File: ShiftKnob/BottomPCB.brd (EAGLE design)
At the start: 37.8 x 40.2 mm, 39 parts, among them IC2 UA78M05DCY, J1 AVR_SPI_PRG_6PTH, Q1 16MHz, Q2 MOSFET-NCHANNELSMD, Q3 MOSFET-PCHANNELSMD, Q4 MOSFET-NCHANNELSMD, Q5 MOSFET-NCHANNELSMD, Q6 MOSFET-NCHANNELSMD, U1 ATMEGA328, U3 FT232RL-BASICSSOP

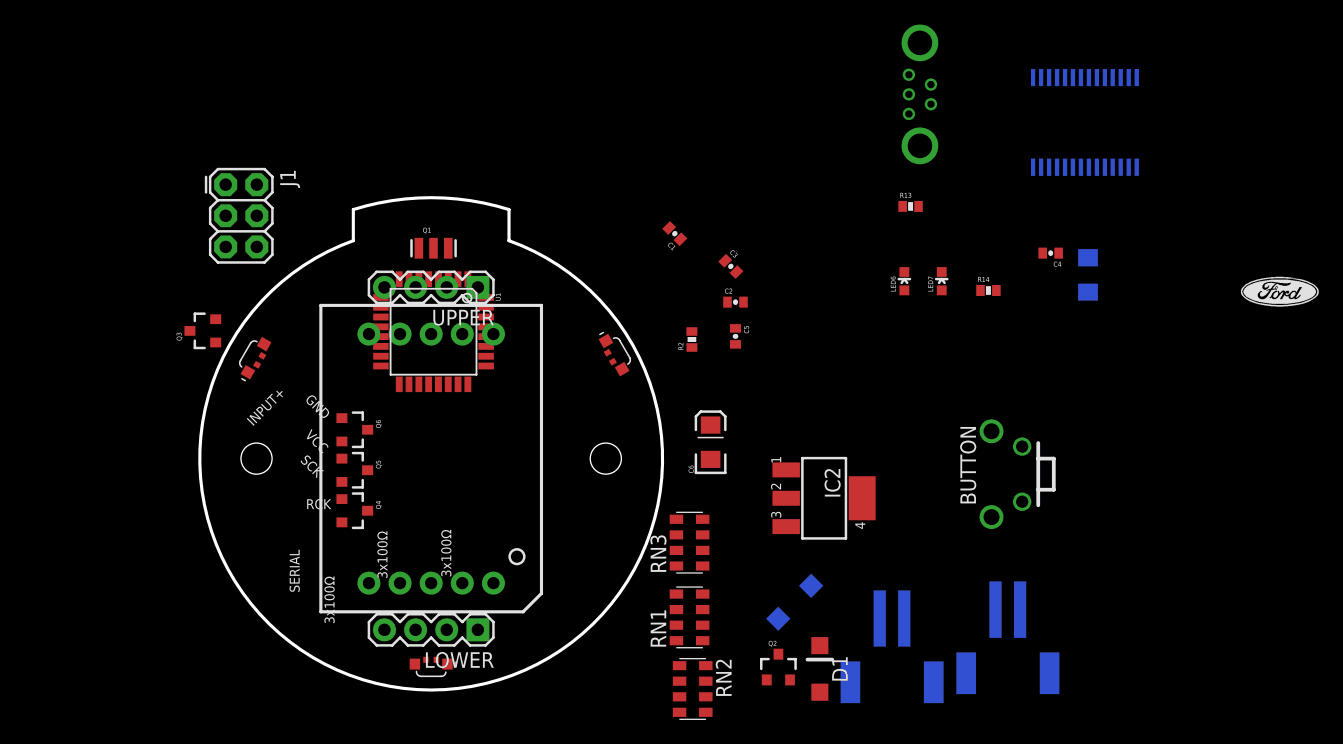
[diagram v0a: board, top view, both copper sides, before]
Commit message: swap out button for edge_mount button in Ford_frames library.
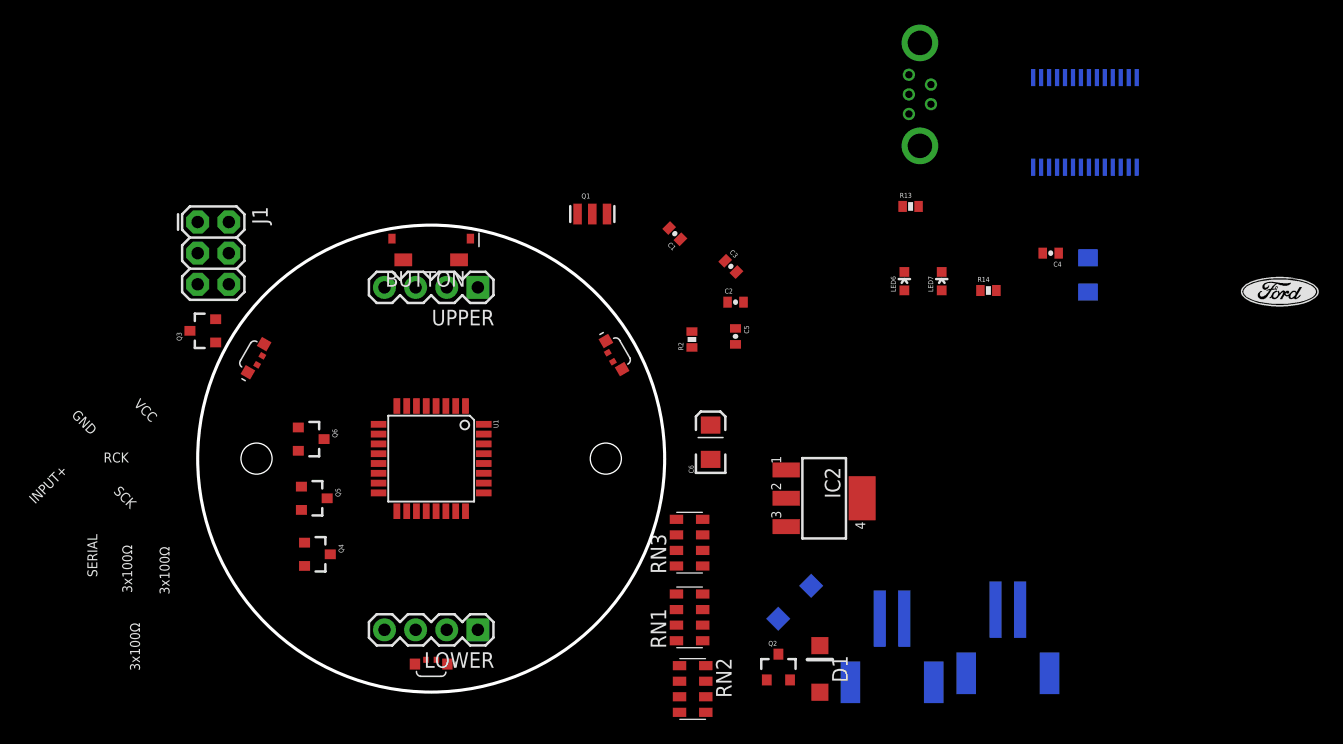
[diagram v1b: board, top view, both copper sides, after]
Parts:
- removed U$2: 7-SEGMENT-DISPLAY-1"-RED, SparkFun-Displays:7-SEGMENT-1"PTH
- BUTTON: value BUTTON_RIGHTANGLE_SMD -> BUTTON_EDGE; device FORD_frames:BUTTON_RIGHTANGLE -> FORD_frames:BUTTON_EDGE
- moved BUTTON 49.9 mm to (21.6, 40.4), turned to 180 degrees
- moved Q1 13.3 mm to (34.7, 41.5)
- moved U1 10.4 mm to (21.6, 21.6)
- moved Q4 4.68 mm to (12.3, 13.8)
- moved Q5 4.02 mm to (12.0, 18.4)
- moved J1 3.81 mm to (2.54, 40.9)
- moved Q6 3.64 mm to (11.8, 23.2)
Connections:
- net D2: now also BUTTON.P2; no longer BUTTON.PIN2
- net GND: now also BUTTON.P1; no longer BUTTON.PIN1
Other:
- board size 37.8 x 40.2 mm -> 38.1 x 38.1 mm

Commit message: everything on the board. need to route traces.
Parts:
- R13, R14: value 1K -> 10K
- moved U3 63.1 mm to (15.2, 28.7), flipped to the top, turned to 0 degrees
- moved C10 53.3 mm to (22.4, 29.2), flipped to the top, turned to 90 degrees
- moved R14 51.4 mm to (15.7, 37.8), turned to 180 degrees
- moved R13 49.0 mm to (12.2, 35.3), turned to 90 degrees
- moved C4 48.5 mm to (24.4, 30.0), turned to 90 degrees
- moved JP4 48.1 mm to (12.4, 16.0), turned to 0 degrees
- moved Q2 47.8 mm to (6.97, 25.4), turned to 180 degrees
- moved LED7 47.8 mm to (15.5, 35.3), turned to 180 degrees
- moved JP3 47.0 mm to (22.8, 15.8), turned to 0 degrees
- moved LED6 46.2 mm to (14.0, 35.3), turned to 180 degrees
- moved IC2 43.3 mm to (10.6, 13.7), turned to 90 degrees
- moved D1 40.7 mm to (12.8, 8.60), turned to 0 degrees
- moved D2 40.5 mm to (12.5, 21.7), flipped to the top, turned to 180 degrees
- moved J1 40.3 mm to (29.0, 10.4), turned to 0 degrees
- moved U$6 40.2 mm to (28.6, 28.1)
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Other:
- board text added: "02"
- board text removed: "01"

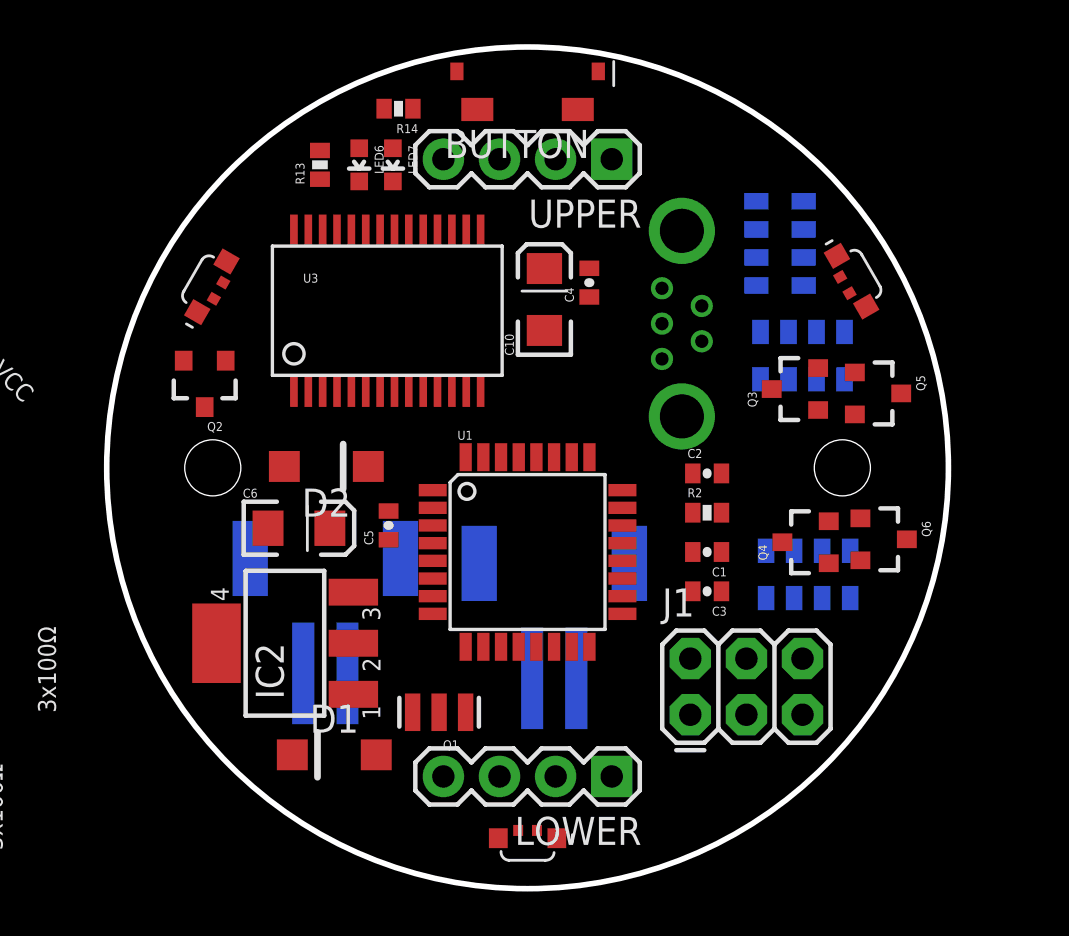
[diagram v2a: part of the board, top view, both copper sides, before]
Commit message: reworked the board layout. power traces complete.
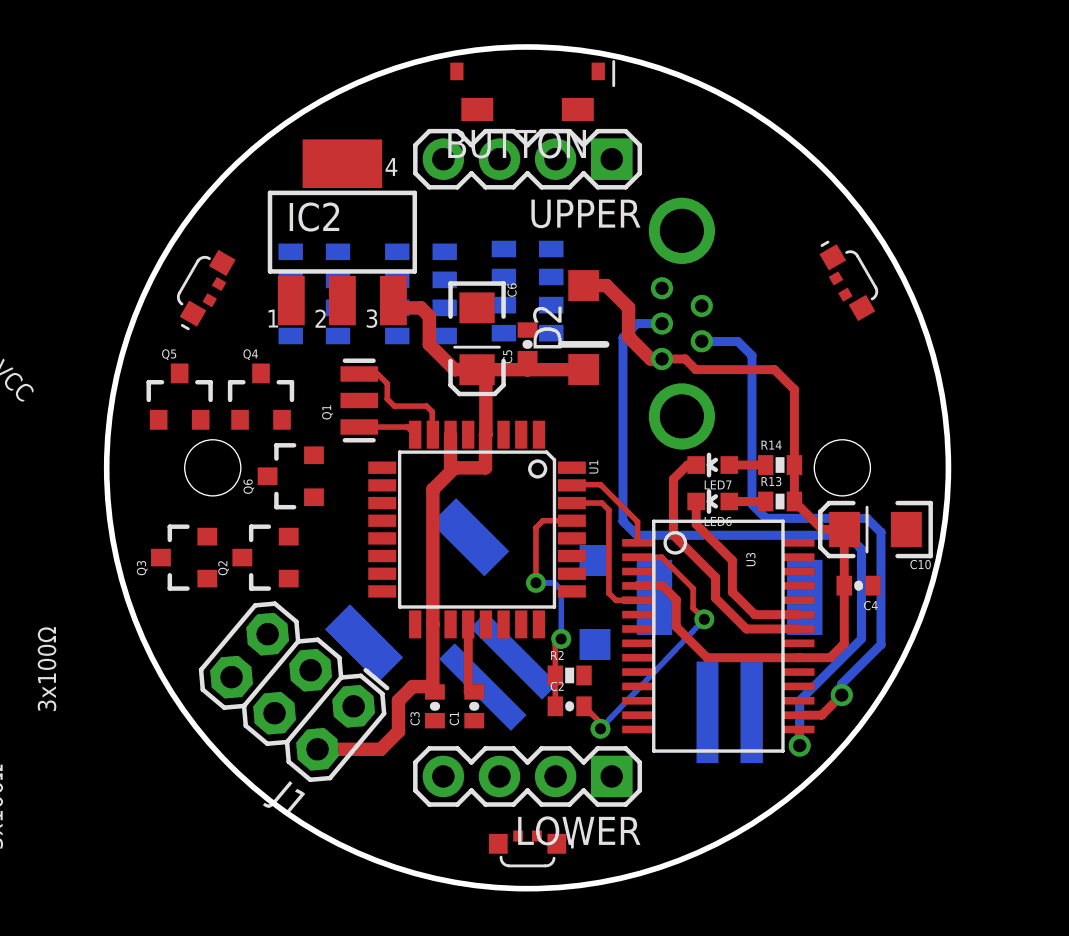
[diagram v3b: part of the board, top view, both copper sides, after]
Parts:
- moved Q5 31.6 mm to (5.84, 24.8), turned to 0 degrees
- moved Q3 28.7 mm to (6.10, 17.5)
- moved Q6 26.9 mm to (10.9, 21.2), turned to 90 degrees
- moved R13 25.8 mm to (33.0, 20.1), turned to 0 degrees
- moved Q4 25.6 mm to (9.53, 24.8), turned to 0 degrees
- moved R14 23.6 mm to (33.0, 21.7), turned to 0 degrees
- moved RN3 22.3 mm to (11.9, 29.5), turned to 90 degrees
- moved LED6 22.1 mm to (30.0, 20.1), turned to 90 degrees
- moved U3 21.0 mm to (30.2, 14.0), turned to 270 degrees
- moved LED7 19.9 mm to (30.0, 21.7), turned to 90 degrees
- moved IC2 18.8 mm to (13.2, 32.3), turned to 0 degrees
- moved C4 18.4 mm to (36.6, 16.3), turned to 180 degrees
- moved C10 18.2 mm to (37.3, 18.8), turned to 180 degrees
- moved RN2 18.1 mm to (21.6, 29.6), turned to 90 degrees
- moved RN1 16.4 mm to (16.8, 29.5)
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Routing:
- net VUSB: track 0.00 -> 37.0 mm
- net VCC: track 0.00 -> 36.9 mm
- net N$21: track 0.00 -> 32.4 mm, vias 0 -> 1
- net N$22: track 0.00 -> 26.1 mm, vias 0 -> 1
- net DTR: track 0.00 -> 12.9 mm, vias 0 -> 2
- net RXLED1: track 0.00 -> 11.8 mm
- net RESET: track 0.00 -> 10.9 mm, vias 0 -> 2
- net TXLED1: track 0.00 -> 8.24 mm
- net RXI: track 0.00 -> 7.00 mm
- net N$2: track 0.00 -> 5.47 mm
- net TXO: track 0.00 -> 4.64 mm
- net AREF: track 0.00 -> 3.33 mm
- net N$1: track 0.00 -> 2.68 mm
- net N$24: track 0.00 -> 1.65 mm
- net N$23: track 0.00 -> 1.65 mm

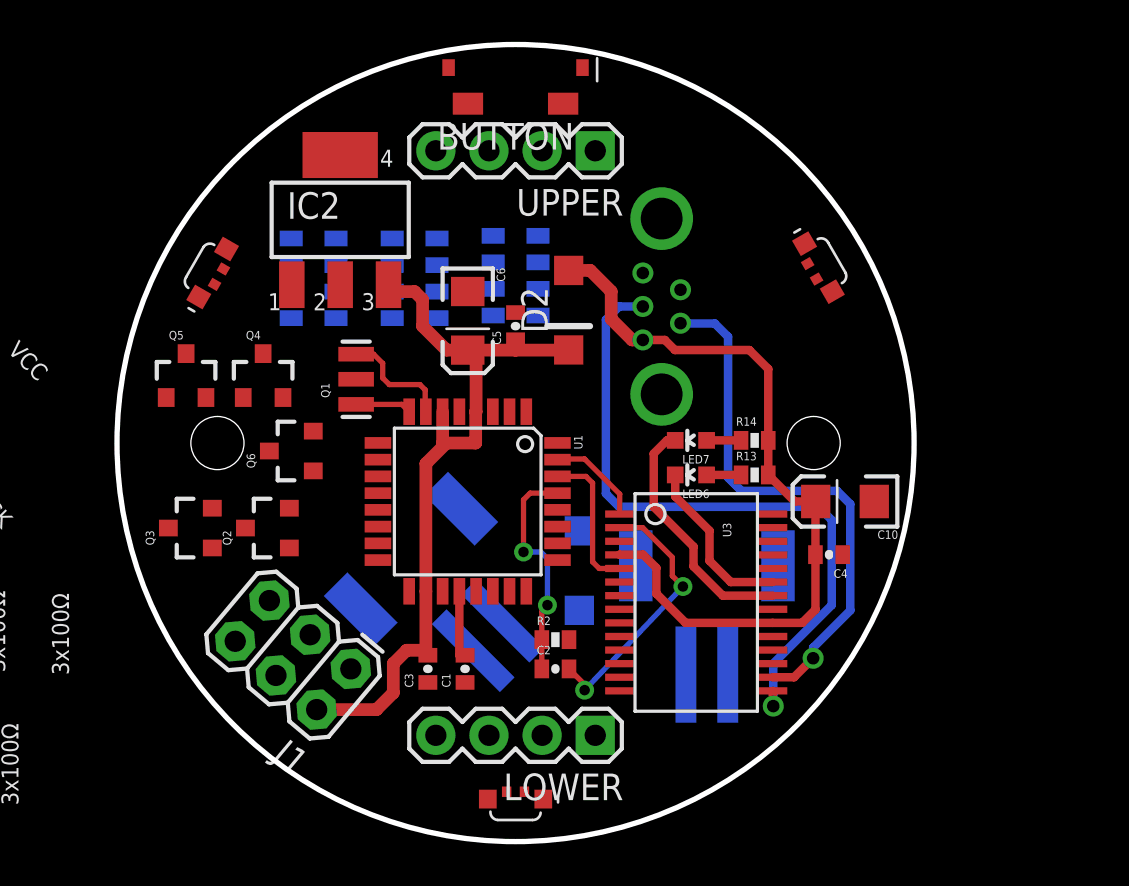
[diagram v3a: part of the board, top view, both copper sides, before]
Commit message: all traces done except motor connection and RGB LEDs.
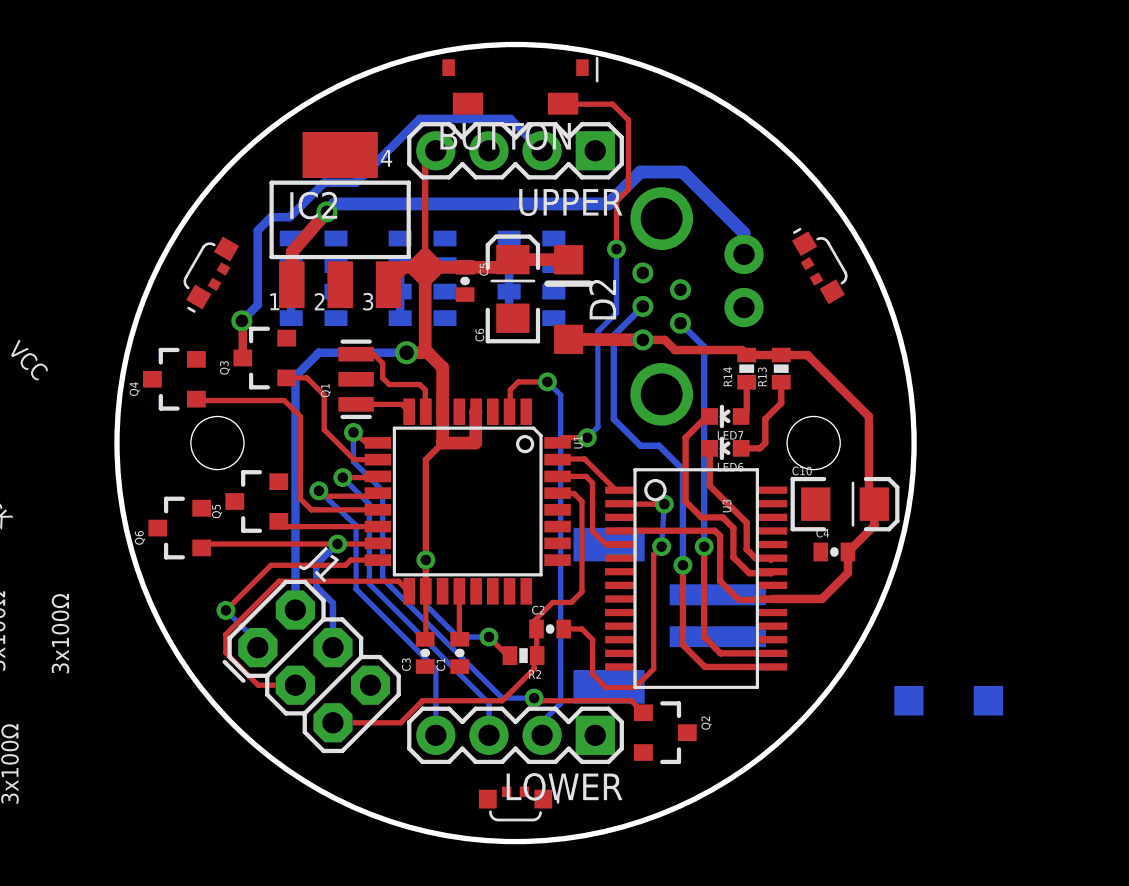
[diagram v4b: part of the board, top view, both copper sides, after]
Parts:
- JP3: device SparkFun-Connectors:JST-2-SMD -> SparkFun-Connectors:1X02
- moved Q2 21.3 mm to (28.7, 7.75), turned to 270 degrees
- moved D1 18.7 mm to (42.3, 9.27), turned to 180 degrees
- moved JP3 16.5 mm to (32.5, 30.6), turned to 270 degrees
- moved JP4 10.0 mm to (27.6, 13.3), turned to 270 degrees
- moved Q3 8.87 mm to (9.65, 25.7)
- moved Q5 6.88 mm to (9.27, 18.8), turned to 90 degrees
- moved Q6 6.48 mm to (5.59, 17.5)
- moved R13 5.24 mm to (34.3, 25.1), turned to 90 degrees
- moved J1 4.56 mm to (9.27, 11.8), turned to 315 degrees
- moved Q4 4.19 mm to (5.33, 24.6), turned to 90 degrees
- moved R14 3.45 mm to (32.6, 25.1), turned to 90 degrees
- moved C5 3.24 mm to (19.2, 29.3), turned to 270 degrees
- moved C6 2.64 mm to (21.5, 29.0), turned to 90 degrees
- moved LED6 2.08 mm to (31.6, 21.3)
- moved LED7 2.01 mm to (31.6, 22.9)
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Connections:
- removed net 3.3V: LED1.2, LED2.2, LED3.2
- net 12V: now also JP3.1; no longer JP3.2
- net D2: now also BUTTON.P1; no longer BUTTON.P2
- net GND: now also BUTTON.P2, JP3.2; no longer BUTTON.P1, JP3.1
- net VCC: now also LED1.2, LED2.2, LED3.2
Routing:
- net VCC: track 36.9 -> 64.7 mm, vias 0 -> 3
- net 12V: track 0.00 -> 27.1 mm, vias 0 -> 1
- net D5/MOTOR: track 0.00 -> 24.0 mm, vias 0 -> 2
- net INPUT+: track 0.00 -> 22.9 mm, vias 0 -> 1
- net D2: track 0.00 -> 20.9 mm, vias 0 -> 2
- net D4/SERIAL: track 0.00 -> 20.5 mm, vias 0 -> 1
- net D8/SCK: track 0.00 -> 17.0 mm, vias 0 -> 1
- net D7/RCK: track 0.00 -> 16.9 mm, vias 0 -> 1
- net D13: track 0.00 -> 14.9 mm
- net N$15: track 0.00 -> 14.2 mm, vias 0 -> 1
- net N$11: track 0.00 -> 13.2 mm
- net RESET: track 10.9 -> 21.5 mm, vias 2 -> 0
- net D12: track 0.00 -> 10.6 mm, vias 0 -> 1
- net N$21: track 32.4 -> 23.4 mm
- net N$22: track 26.1 -> 19.1 mm
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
